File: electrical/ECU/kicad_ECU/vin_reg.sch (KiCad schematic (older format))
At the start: 10 parts

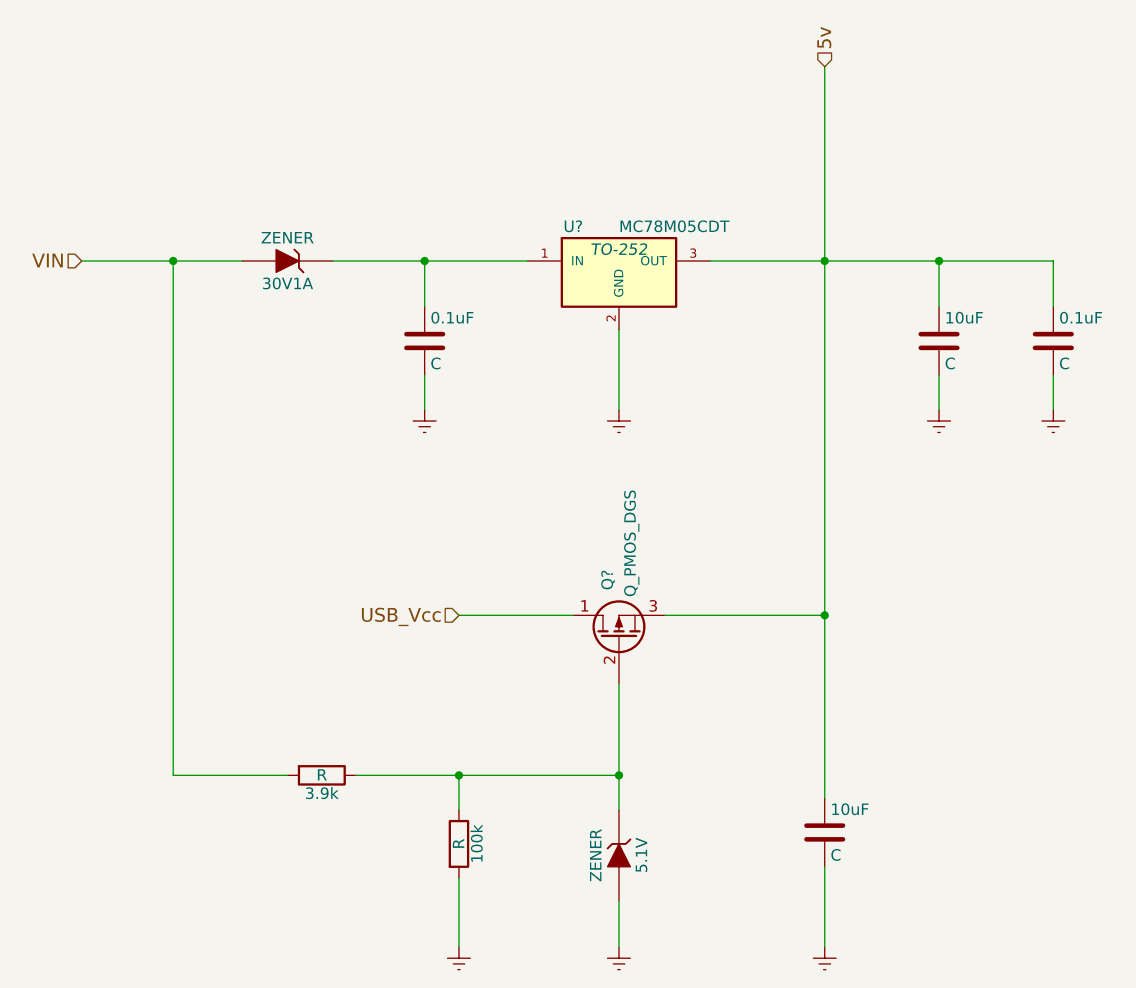
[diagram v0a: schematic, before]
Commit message: fixed some naming errors and initial round of double checking
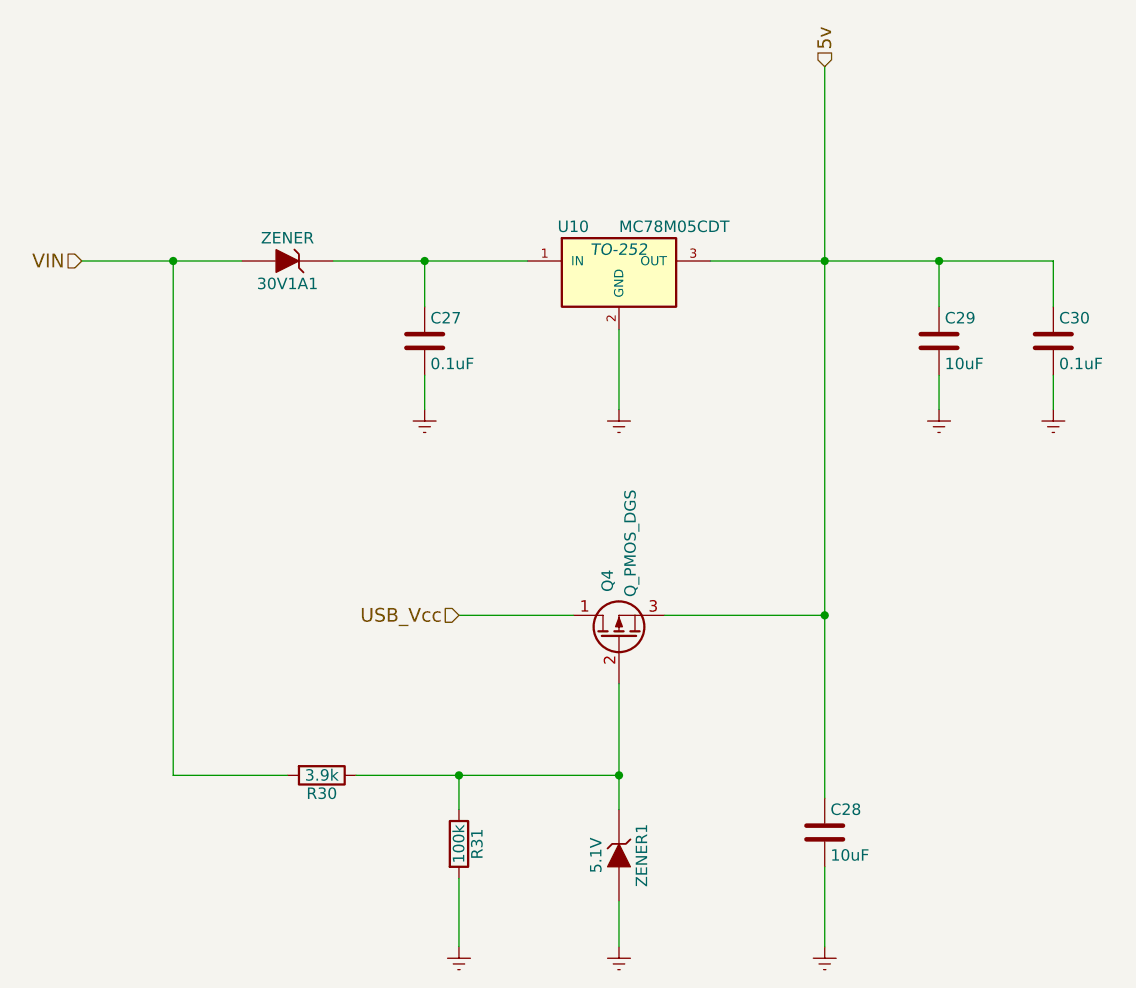
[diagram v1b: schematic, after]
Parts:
- C27, C30: renamed from 0.1uF; value C -> 0.1uF
- C28, C29: renamed from 10uF; value C -> 10uF
- R30: renamed from 3.9k; value R -> 3.9k
- R31: renamed from 100k; value R -> 100k
- ZENER1: renamed from 5.1V; value ZENER -> 5.1V
- gave numbers to parts that had none: 2
- renumbered 30V1A to 30V1A1
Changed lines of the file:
@@
 5v
 $Comp
-L ZENER 30V1A
+L ZENER 30V1A1
 U 1 1 598E15FE
 P 4050 2550
-F 0 "30V1A" H 4050 2650 50  0000 C CNN
+F 0 "30V1A1" H 4050 2650 50  0000 C CNN
 F 1 "ZENER" H 4050 2450 50  0000 C CNN
 F 2 "" H 4050 2550 50  0000 C CNN
@@
 $EndComp
 $Comp
-L MC78M05CDT U?
+L MC78M05CDT U10
 U 1 1 598E1622
 P 5500 2600
-F 0 "U?" H 5300 2800 50  0000 C CNN
+F 0 "U10" H 5300 2800 50  0000 C CNN
 F 1 "MC78M05CDT" H 5500 2800 50  0000 L CNN
 F 2 "TO-252" H 5500 2700 50  0000 C CIN
@@
 $EndComp
 $Comp
-L C 0.1uF
+L C C27
 U 1 1 598E1651
 P 4650 2900
-F 0 "0.1uF" H 4675 3000 50  0000 L CNN
-F 1 "C" H 4675 2800 50  0000 L CNN
+F 0 "C27" H 4675 3000 50  0000 L CNN
+F 1 "0.1uF" H 4675 2800 50  0000 L CNN
 F 2 "" H 4688 2750 50  0000 C CNN
 F 3 "" H 4650 2900 50  0000 C CNN
@@
 $EndComp
 $Comp
-L C 10uF
+L C C29
 U 1 1 598E1685
 P 6900 2900
-F 0 "10uF" H 6925 3000 50  0000 L CNN
-F 1 "C" H 6925 2800 50  0000 L CNN
+F 0 "C29" H 6925 3000 50  0000 L CNN
+F 1 "10uF" H 6925 2800 50  0000 L CNN
 F 2 "" H 6938 2750 50  0000 C CNN
 F 3 "" H 6900 2900 50  0000 C CNN
@@
 $EndComp
 $Comp
-L C 0.1uF
+L C C30
 U 1 1 598E16FC
 P 7400 2900
-F 0 "0.1uF" H 7425 3000 50  0000 L CNN
-F 1 "C" H 7425 2800 50  0000 L CNN
+F 0 "C30" H 7425 3000 50  0000 L CNN
+F 1 "0.1uF" H 7425 2800 50  0000 L CNN
 F 2 "" H 7438 2750 50  0000 C CNN
 F 3 "" H 7400 2900 50  0000 C CNN
@@
 $EndComp
 $Comp
-L Q_PMOS_DGS Q?
+L Q_PMOS_DGS Q4
 U 1 1 598E1750
 P 5500 4200
-F 0 "Q?" H 5800 4250 50  0000 R CNN
+F 0 "Q4" H 5800 4250 50  0000 R CNN
 F 1 "Q_PMOS_DGS" H 6150 4150 50  0000 R CNN
 F 2 "" H 5700 4300 50  0000 C CNN
@@
 $EndComp
 $Comp
-L ZENER 5.1V
+L ZENER ZENER1
 U 1 1 598E17AF
 P 5500 5150
-F 0 "5.1V" H 5500 5250 50  0000 C CNN
-F 1 "ZENER" H 5500 5050 50  0000 C CNN
+F 0 "ZENER1" H 5500 5250 50  0000 C CNN
+F 1 "5.1V" H 5500 5050 50  0000 C CNN
 F 2 "" H 5500 5150 50  0000 C CNN
 F 3 "" H 5500 5150 50  0000 C CNN
@@
 $EndComp
 $Comp
-L R 100k
+L R R31
 U 1 1 598E17EF
 P 4800 5100
-F 0 "100k" V 4880 5100 50  0000 C CNN
-F 1 "R" V 4800 5100 50  0000 C CNN
+F 0 "R31" V 4880 5100 50  0000 C CNN
+F 1 "100k" V 4800 5100 50  0000 C CNN
 F 2 "" V 4730 5100 50  0000 C CNN
 F 3 "" H 4800 5100 50  0000 C CNN
@@
 $EndComp
 $Comp
-L R 3.9k
+L R R30
 U 1 1 598E182B
 P 4200 4800
-F 0 "3.9k" V 4280 4800 50  0000 C CNN
-F 1 "R" V 4200 4800 50  0000 C CNN
+F 0 "R30" V 4280 4800 50  0000 C CNN
+F 1 "3.9k" V 4200 4800 50  0000 C CNN
 F 2 "" V 4130 4800 50  0000 C CNN
 F 3 "" H 4200 4800 50  0000 C CNN
@@
 $EndComp
 $Comp
-L C 10uF
+L C C28
 U 1 1 598E186D
 P 6400 5050
-F 0 "10uF" H 6425 5150 50  0000 L CNN
-F 1 "C" H 6425 4950 50  0000 L CNN
+F 0 "C28" H 6425 5150 50  0000 L CNN
+F 1 "10uF" H 6425 4950 50  0000 L CNN
 F 2 "" H 6438 4900 50  0000 C CNN
 F 3 "" H 6400 5050 50  0000 C CNN
@@
 Connection ~ 4800 4800
 $Comp
-L Earth #PWR?
+L Earth #PWR32
 U 1 1 598E1983
 P 4650 3200
-F 0 "#PWR?" H 4650 2950 50  0001 C CNN
+F 0 "#PWR32" H 4650 2950 50  0001 C CNN
 F 1 "Earth" H 4650 3050 50  0001 C CNN
 F 2 "" H 4650 3200 50  0000 C CNN
@@
 $EndComp
 $Comp
-L Earth #PWR?
+L Earth #PWR34
 U 1 1 598E19AB
 P 5500 3200
-F 0 "#PWR?" H 5500 2950 50  0001 C CNN
+F 0 "#PWR34" H 5500 2950 50  0001 C CNN
 F 1 "Earth" H 5500 3050 50  0001 C CNN
 F 2 "" H 5500 3200 50  0000 C CNN
@@
 $EndComp
 $Comp
-L Earth #PWR?
+L Earth #PWR37
 U 1 1 598E19D3
 P 6900 3200
-F 0 "#PWR?" H 6900 2950 50  0001 C CNN
+F 0 "#PWR37" H 6900 2950 50  0001 C CNN
 F 1 "Earth" H 6900 3050 50  0001 C CNN
 F 2 "" H 6900 3200 50  0000 C CNN
@@
 $EndComp
 $Comp
-L Earth #PWR?
+L Earth #PWR38
 U 1 1 598E19FB
 P 7400 3200
-F 0 "#PWR?" H 7400 2950 50  0001 C CNN
+F 0 "#PWR38" H 7400 2950 50  0001 C CNN
 F 1 "Earth" H 7400 3050 50  0001 C CNN
 F 2 "" H 7400 3200 50  0000 C CNN
@@
 $EndComp
 $Comp
-L Earth #PWR?
+L Earth #PWR33
 U 1 1 598E1A23
 P 4800 5550
-F 0 "#PWR?" H 4800 5300 50  0001 C CNN
+F 0 "#PWR33" H 4800 5300 50  0001 C CNN
 F 1 "Earth" H 4800 5400 50  0001 C CNN
 F 2 "" H 4800 5550 50  0000 C CNN
@@
 $EndComp
 $Comp
-L Earth #PWR?
+L Earth #PWR35
 U 1 1 598E1A4B
 P 5500 5550
-F 0 "#PWR?" H 5500 5300 50  0001 C CNN
+F 0 "#PWR35" H 5500 5300 50  0001 C CNN
 F 1 "Earth" H 5500 5400 50  0001 C CNN
 F 2 "" H 5500 5550 50  0000 C CNN
@@
 $EndComp
 $Comp
-L Earth #PWR?
+L Earth #PWR36
 U 1 1 598E1A73
 P 6400 5550
-F 0 "#PWR?" H 6400 5300 50  0001 C CNN
+F 0 "#PWR36" H 6400 5300 50  0001 C CNN
 F 1 "Earth" H 6400 5400 50  0001 C CNN
 F 2 "" H 6400 5550 50  0000 C CNN
